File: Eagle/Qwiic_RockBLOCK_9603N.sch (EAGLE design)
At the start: 54 parts, among them J1 SS4-10-3.50-X-D, J3 PTH, J6 ISP, J7 U.FL, Q1 DMG3415U-7, Q2 2N2222, U1 ATTINY84-ARDUINO, U2 LTC3225EDDB#TRMPBF

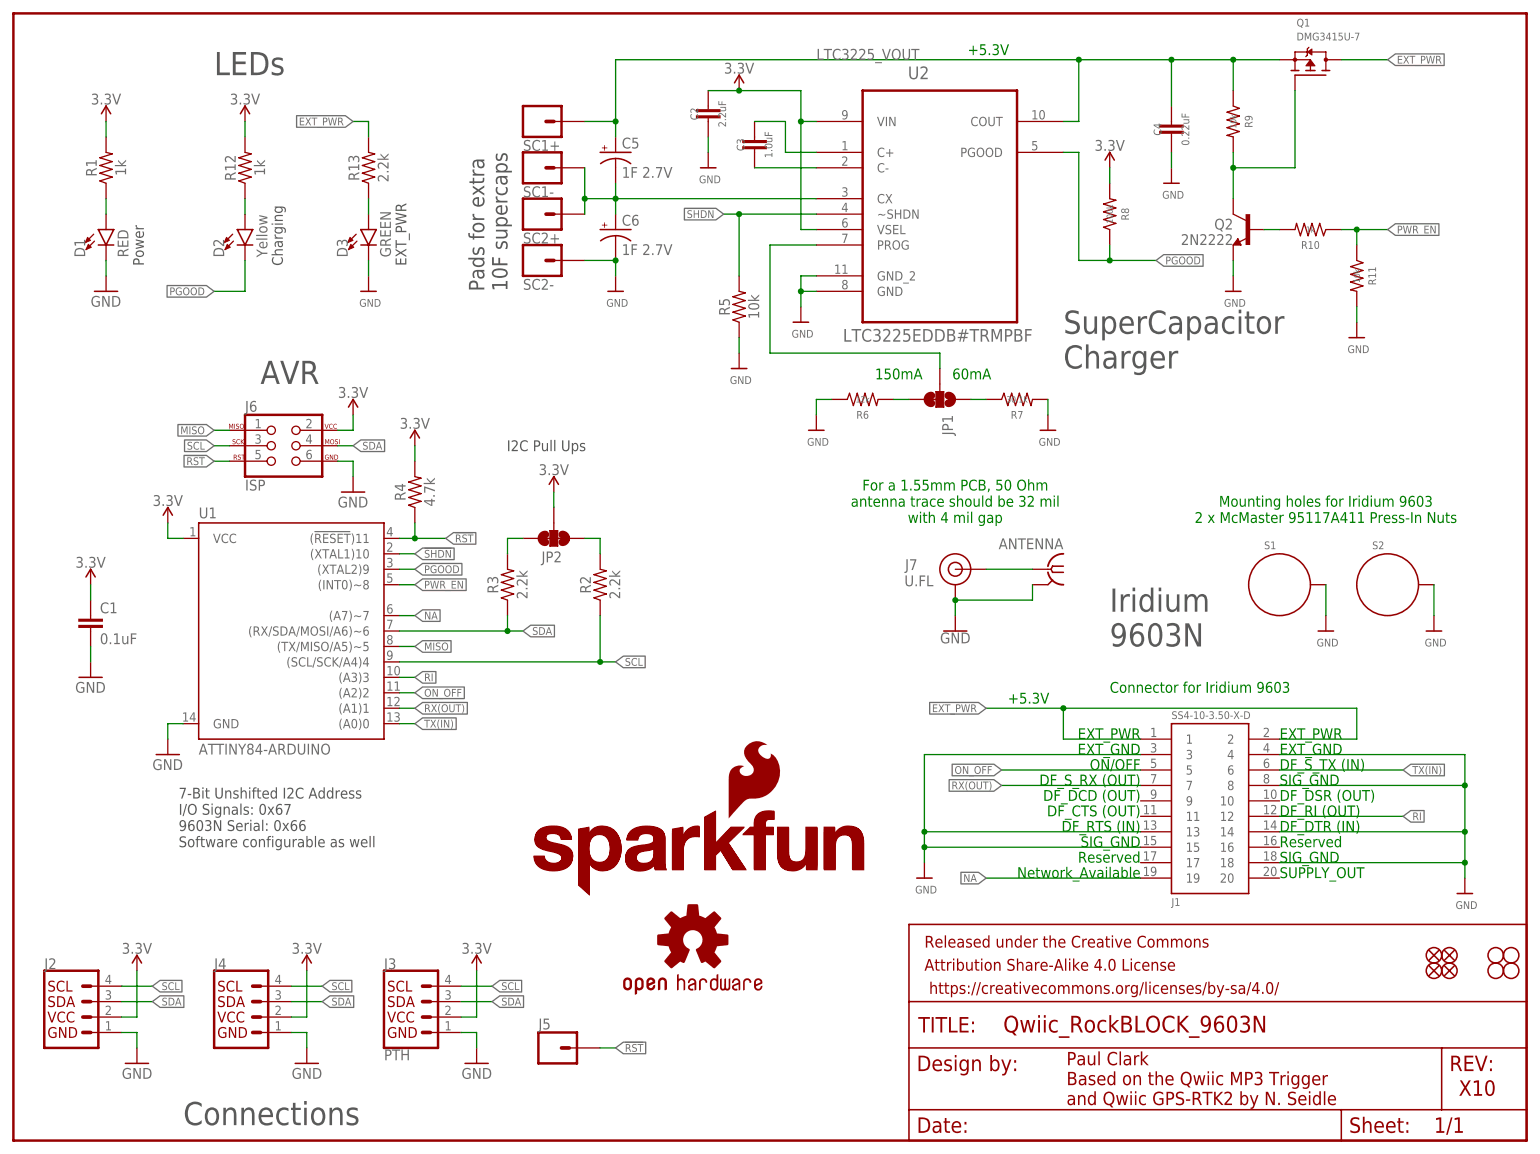
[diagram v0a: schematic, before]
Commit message: Updated the PCB and included the Arduino code
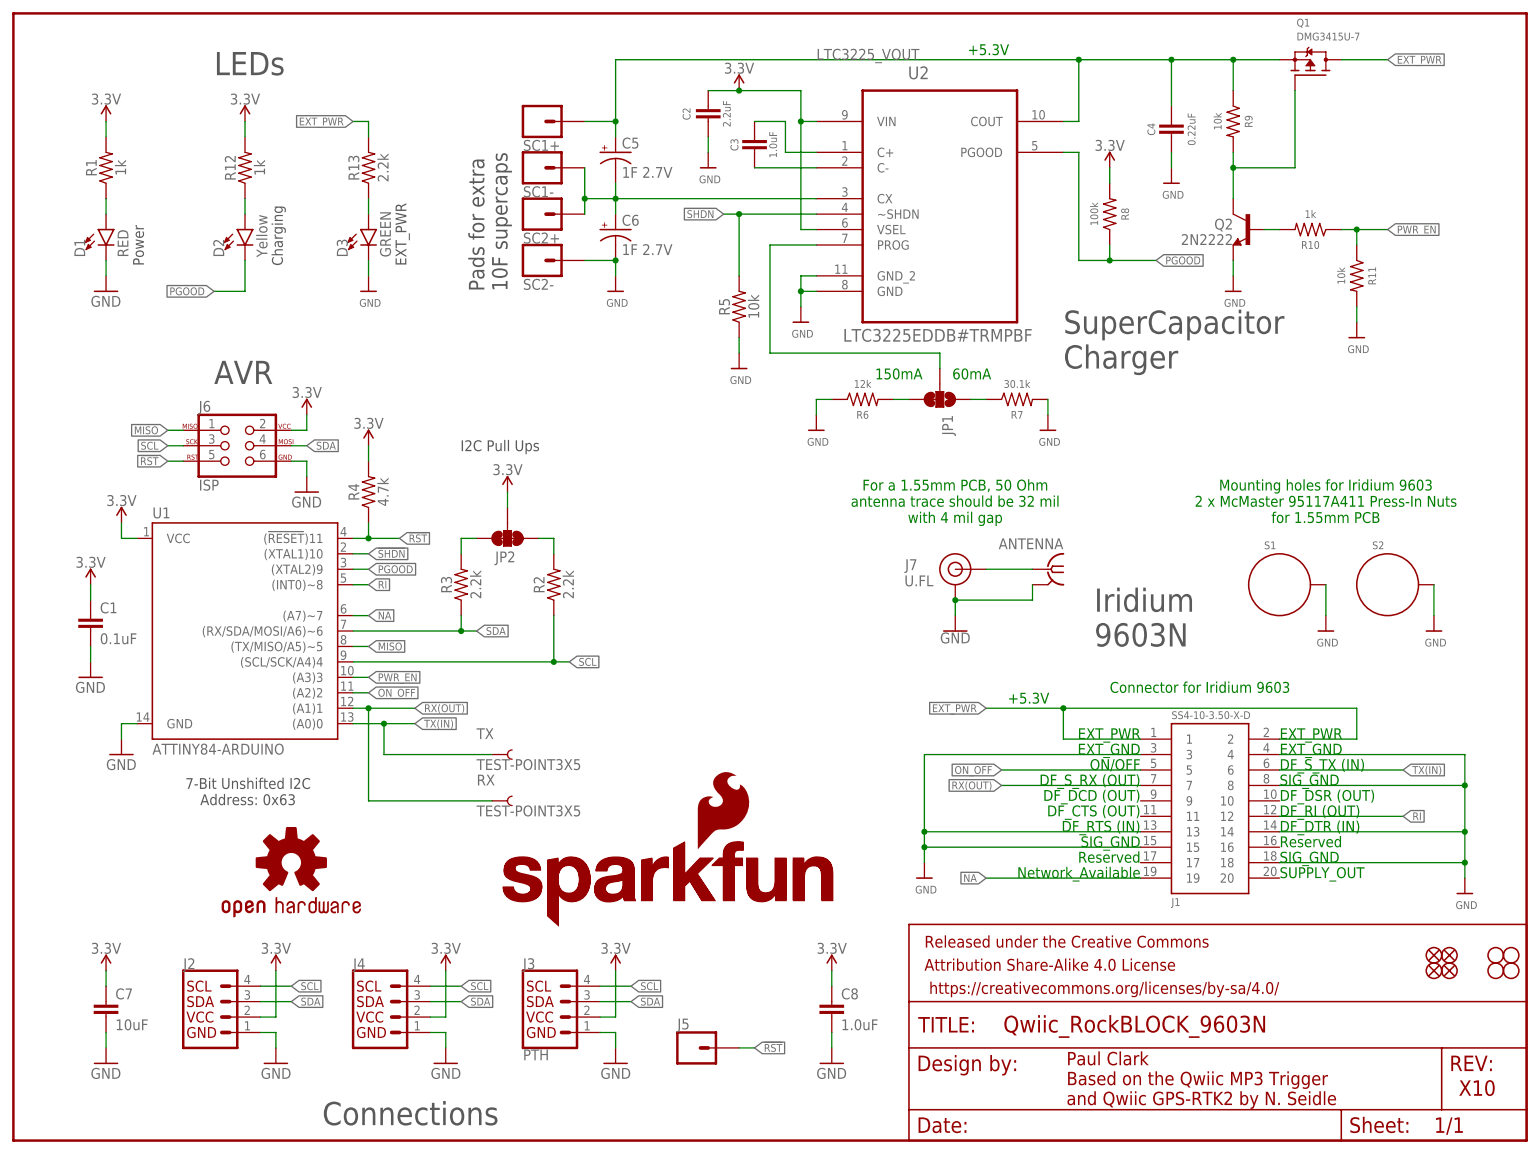
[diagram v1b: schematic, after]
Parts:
- added C7: 10uF, SparkFun-Capacitors:10UF-0603-6.3V-20%
- added C8: 1.0uF, SparkFun-Capacitors:1.0UF-0603-16V-10%
- added RX, TX: TEST-POINT3X5, SparkFun-Connectors:TEST-POINT3X5
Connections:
- net 3.3V: now also C7.1, C8.1
- net GND: now also C7.2, C8.2
- net PWR_EN: now also U1.(A3)3; no longer U1.(INT0)~8
- net RI: now also U1.(INT0)~8; no longer U1.(A3)3
- net RX(OUT): now also RX.1
- net TX(IN): now also TX.1
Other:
- note added: "7-Bit Unshifted I2C Address: 0x63"
- note added: "Mounting holes for Iridium 9603 2 x McMaster 95117A411 Press-In Nuts for 1.55mm PCB"
- note removed: "7-Bit Unshifted I2C Address I/O Signals: 0x67 9603N Serial: 0x66 Software configurable as well"
- note removed: "Mounting holes for Iridium 9603 2 x McMaster 95117A411 Press-In Nuts"
- moved on the sheet: J2, J3, J4, J5, J6, JP2, R2, R3, R4, U1
